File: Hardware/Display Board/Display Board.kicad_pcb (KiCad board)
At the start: 2 copper layers, 165.1 x 88.9 mm, 44 parts, among them J1 GPS, J10 Conn_02x03_Odd_Even, J11 Conn_02x03_Odd_Even, J12 Conn_02x03_Odd_Even, J13 Conn_02x03_Odd_Even, J14 Conn_02x03_Odd_Even, J15 Conn_02x03_Odd_Even, J16 Conn_02x03_Odd_Even, J17 Conn_02x03_Odd_Even, J18 Conn_02x03_Odd_Even, J19 Conn_02x03_Odd_Even, J2 RTC, J20 Conn_02x03_Odd_Even, J21 Conn_02x03_Odd_Even, J22 Conn_02x03_Odd_Even, J23 Conn_02x03_Odd_Even, J24 Conn_02x03_Odd_Even, J25 Conn_02x03_Odd_Even, J26 Conn_02x03_Odd_Even, J27 Conn_02x03_Odd_Even, J28 Conn_02x03_Odd_Even, J29 Conn_02x03_Odd_Even, J3 CONT, J30 Conn_02x03_Odd_Even, J31 Conn_02x03_Odd_Even, J4 H:M, J5 M:D, J6 M:S, J7 D:Y, J8 Conn_02x03_Odd_Even, J9 Conn_02x03_Odd_Even

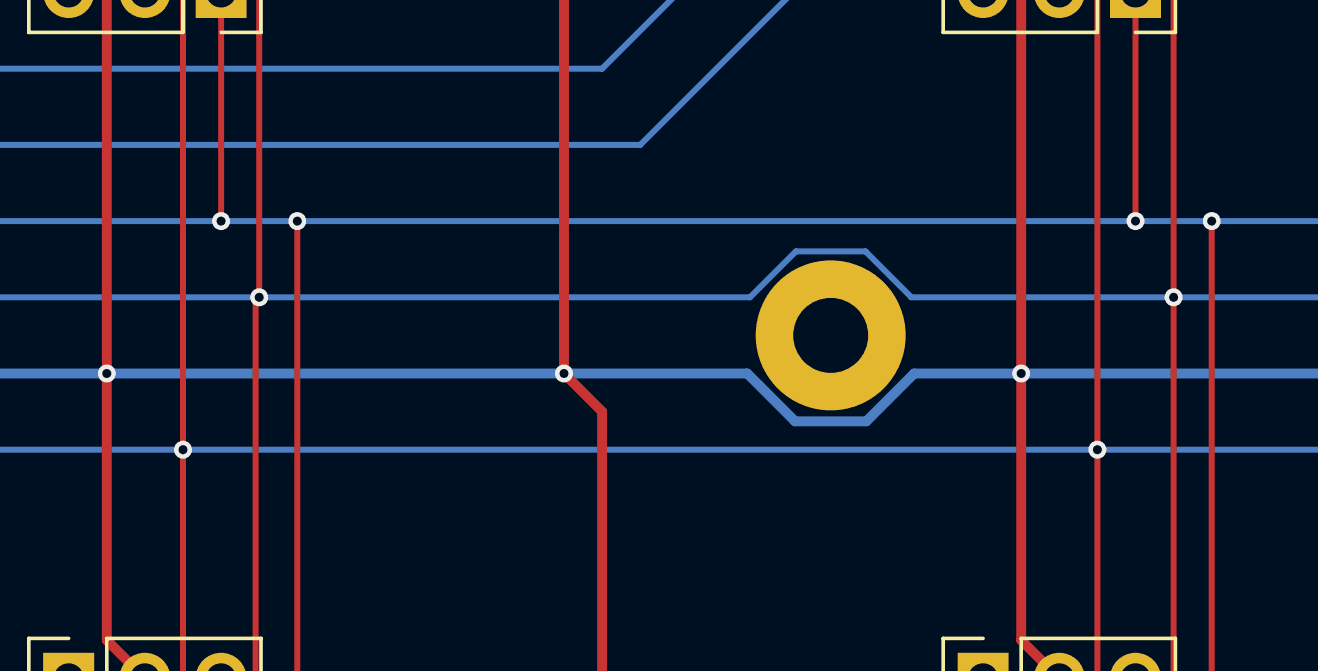
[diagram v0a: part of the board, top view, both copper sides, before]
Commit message: Cleaned up the copper pour
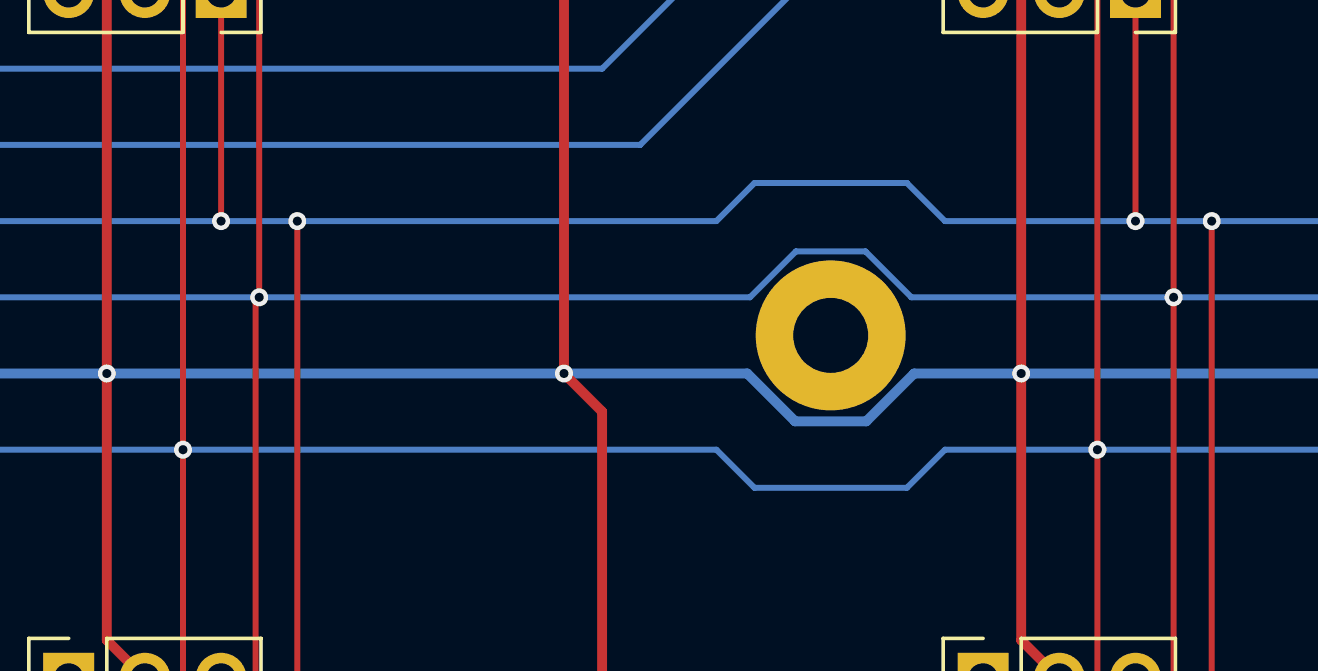
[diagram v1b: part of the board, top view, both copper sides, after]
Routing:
- net Vdd: track 500.1 -> 501.2 mm
- net SDA: track 481.8 -> 482.9 mm
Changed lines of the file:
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@@
+	)
+	(segment
+		(start 124.46 111.76)
+		(end 129.54 111.76)
+		(width 0.2)
+		(layer "B.Cu")
+		(net 2)
 	)
 	(segment
@@
 	)
 	(segment
-		(start 99.06 111.76)
-		(end 129.54 111.76)
+		(start 118.11 113.03)
+		(end 123.19 113.03)
+		(width 0.2)
+		(layer "B.Cu")
+		(net 2)
+	)
+	(segment
+		(start 123.19 113.03)
+		(end 124.46 111.76)
 		(width 0.2)
 		(layer "B.Cu")
@@
 	)
 	(segment
+		(start 116.84 111.76)
+		(end 118.11 113.03)
+		(width 0.2)
+		(layer "B.Cu")
+		(net 2)
+	)
+	(segment
 		(start 152.4 111.76)
 		(end 182.88 111.76)
@@
 	)
 	(segment
+		(start 99.06 111.76)
+		(end 116.84 111.76)
+		(width 0.2)
+		(layer "B.Cu")
+		(net 2)
+	)
+	(segment
 		(start 111.76 82.55)
 		(end 111.76 109.22)
@@
 	)
 	(segment
-		(start 102.87 104.14)
-		(end 130.81 104.14)
+		(start 123.19 102.87)
+		(end 124.46 104.14)
 		(width 0.2)
 		(layer "B.Cu")
@@
 	)
 	(segment
+		(start 124.46 104.14)
+		(end 130.81 104.14)
+		(width 0.2)
+		(layer "B.Cu")
+		(net 8)
+	)
+	(segment
 		(start 207.01 104.14)
 		(end 209.55 104.14)
@@
 	)
 	(segment
+		(start 102.87 104.14)
+		(end 116.84 104.14)
+		(width 0.2)
+		(layer "B.Cu")
+		(net 8)
+	)
+	(segment
 		(start 153.67 104.14)
 		(end 156.21 104.14)
@@
 	)
 	(segment
+		(start 116.84 104.14)
+		(end 118.11 102.87)
+		(width 0.2)
+		(layer "B.Cu")
+		(net 8)
+	)
+	(segment
 		(start 184.15 104.14)
 		(end 186.69 104.14)
+		(width 0.2)
+		(layer "B.Cu")
+		(net 8)
+	)
+	(segment
+		(start 118.11 102.87)
+		(end 123.19 102.87)
 		(width 0.2)
 		(layer "B.Cu")
@@
 			(thermal_gap 0.5)
 			(thermal_bridge_width 0.5)
-			(island_removal_mode 1)
+			(island_removal_mode 2)
 			(island_area_min 9.999999)
 		)

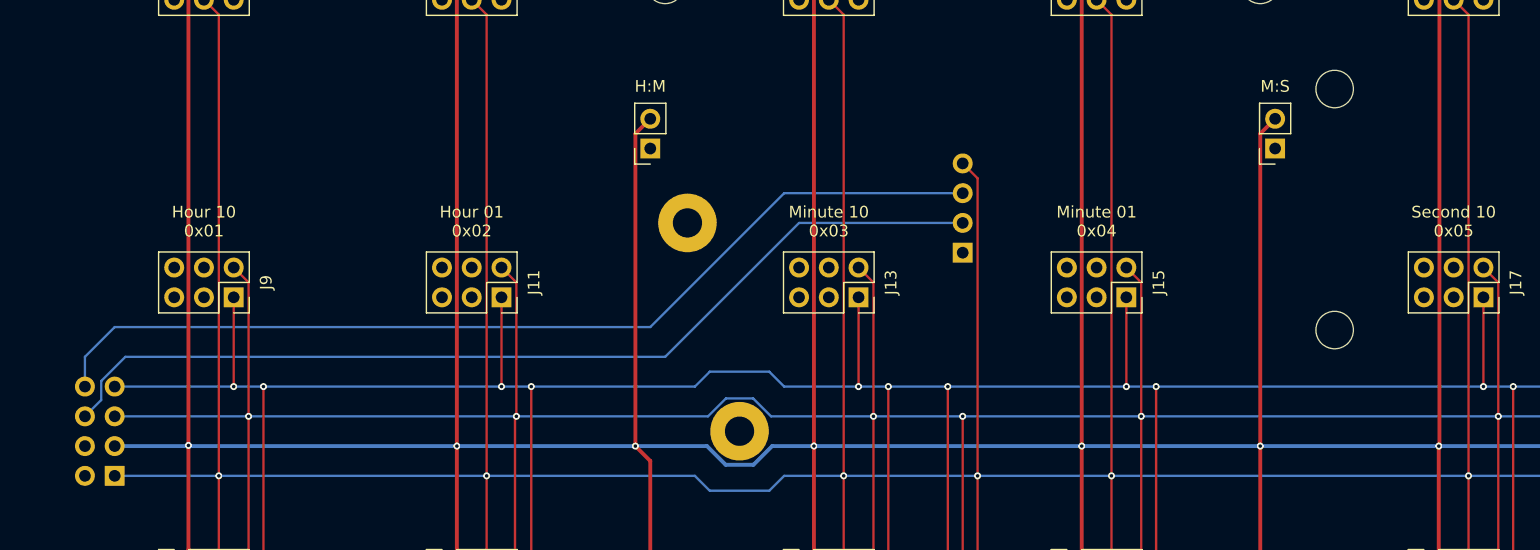
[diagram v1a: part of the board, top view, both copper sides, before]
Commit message: Rotated GPS module for better antenna routing
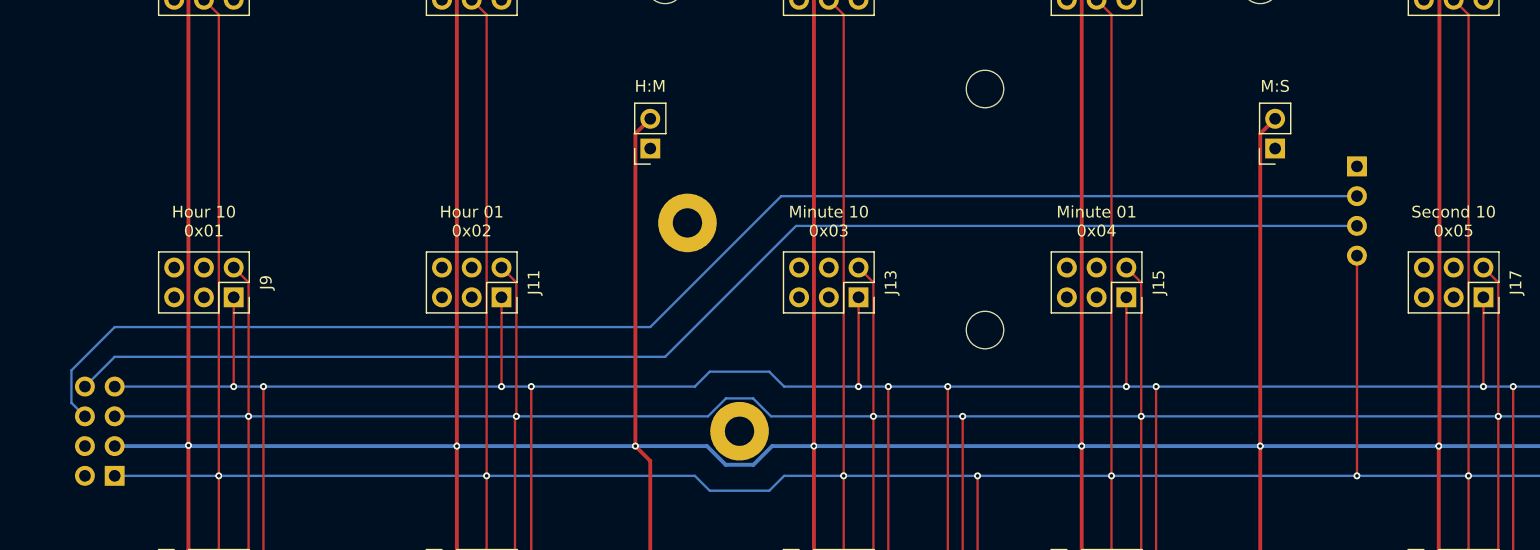
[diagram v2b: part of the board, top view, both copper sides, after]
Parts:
- J3: value CONT -> CONTROLLER
- moved H3 36.2 mm to (141.6, 99.3), turned to 180 degrees
- moved H6 36.2 mm to (141.6, 78.7), turned to 180 degrees
- moved J1 34.5 mm to (173.4, 85.3), turned to 180 degrees
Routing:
- net MCU RX / GPS TX: track 82.7 -> 120.3 mm
- net MCU TX / GPS RX: track 83.3 -> 114.3 mm
- net Vdd: track 501.2 -> 492.8 mm, vias 7 -> 8
